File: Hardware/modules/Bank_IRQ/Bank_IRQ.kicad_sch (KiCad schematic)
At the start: 28 parts, among them J1 Ports, J2 Bus_PCI_6502, U1 74HC00, U2 74HC138, U3 6525

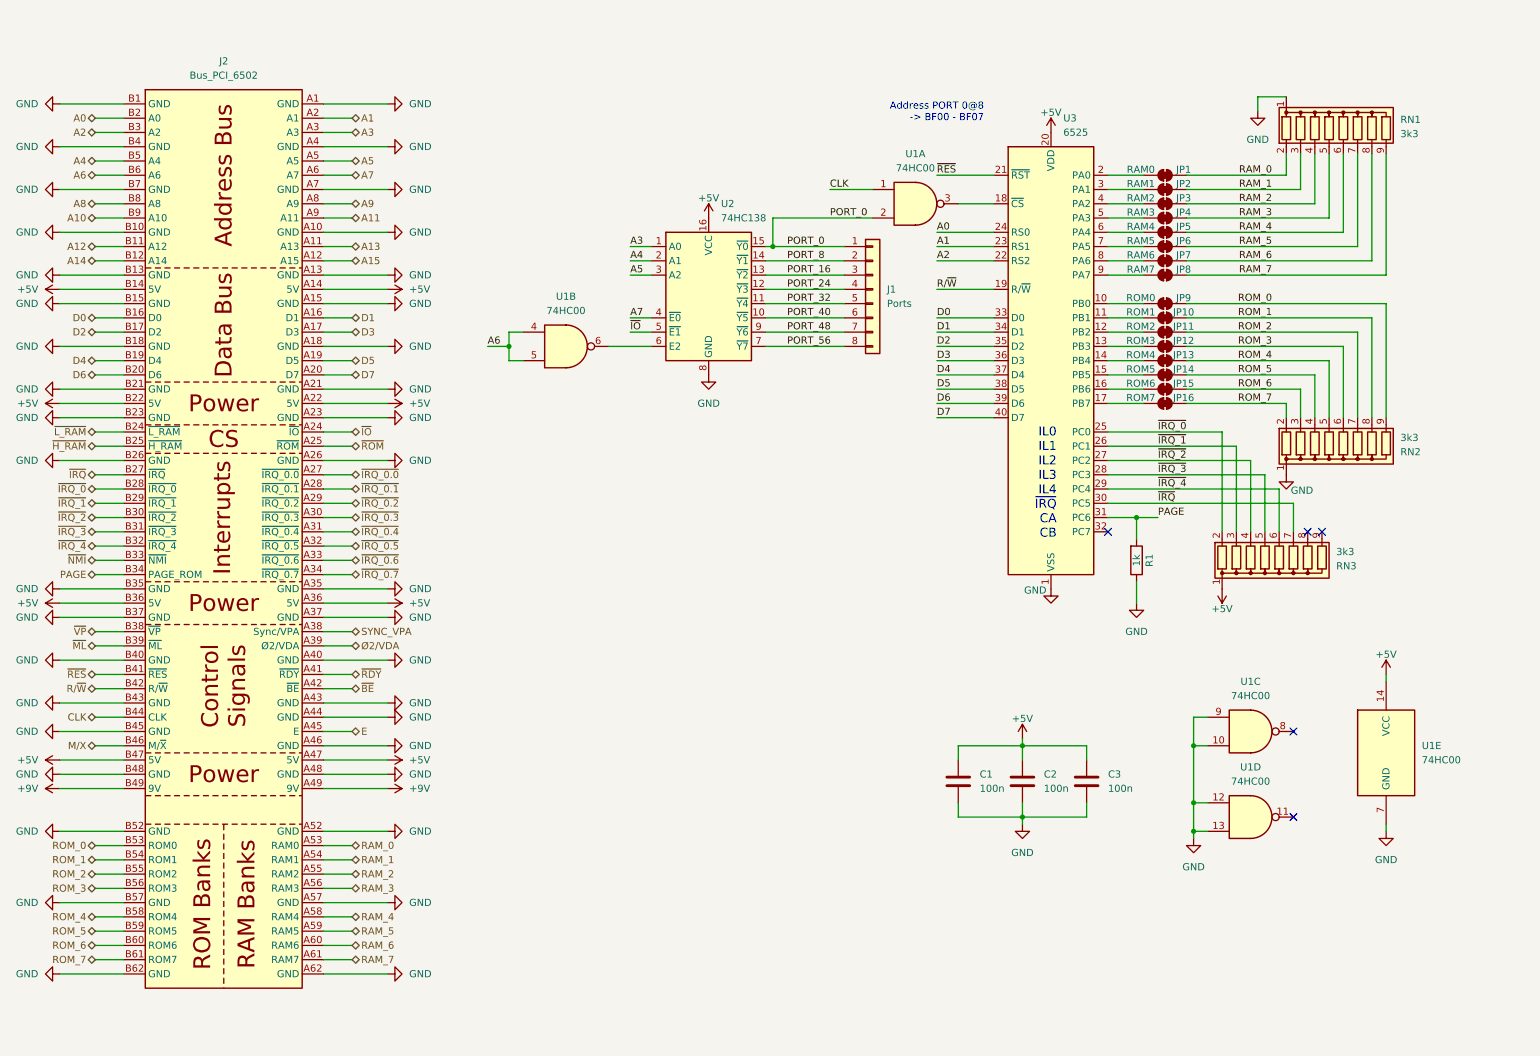
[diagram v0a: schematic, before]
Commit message: Hardware Update Add MyCPU VGA Module Beautify all Schematics minor Error corrections Readme Update
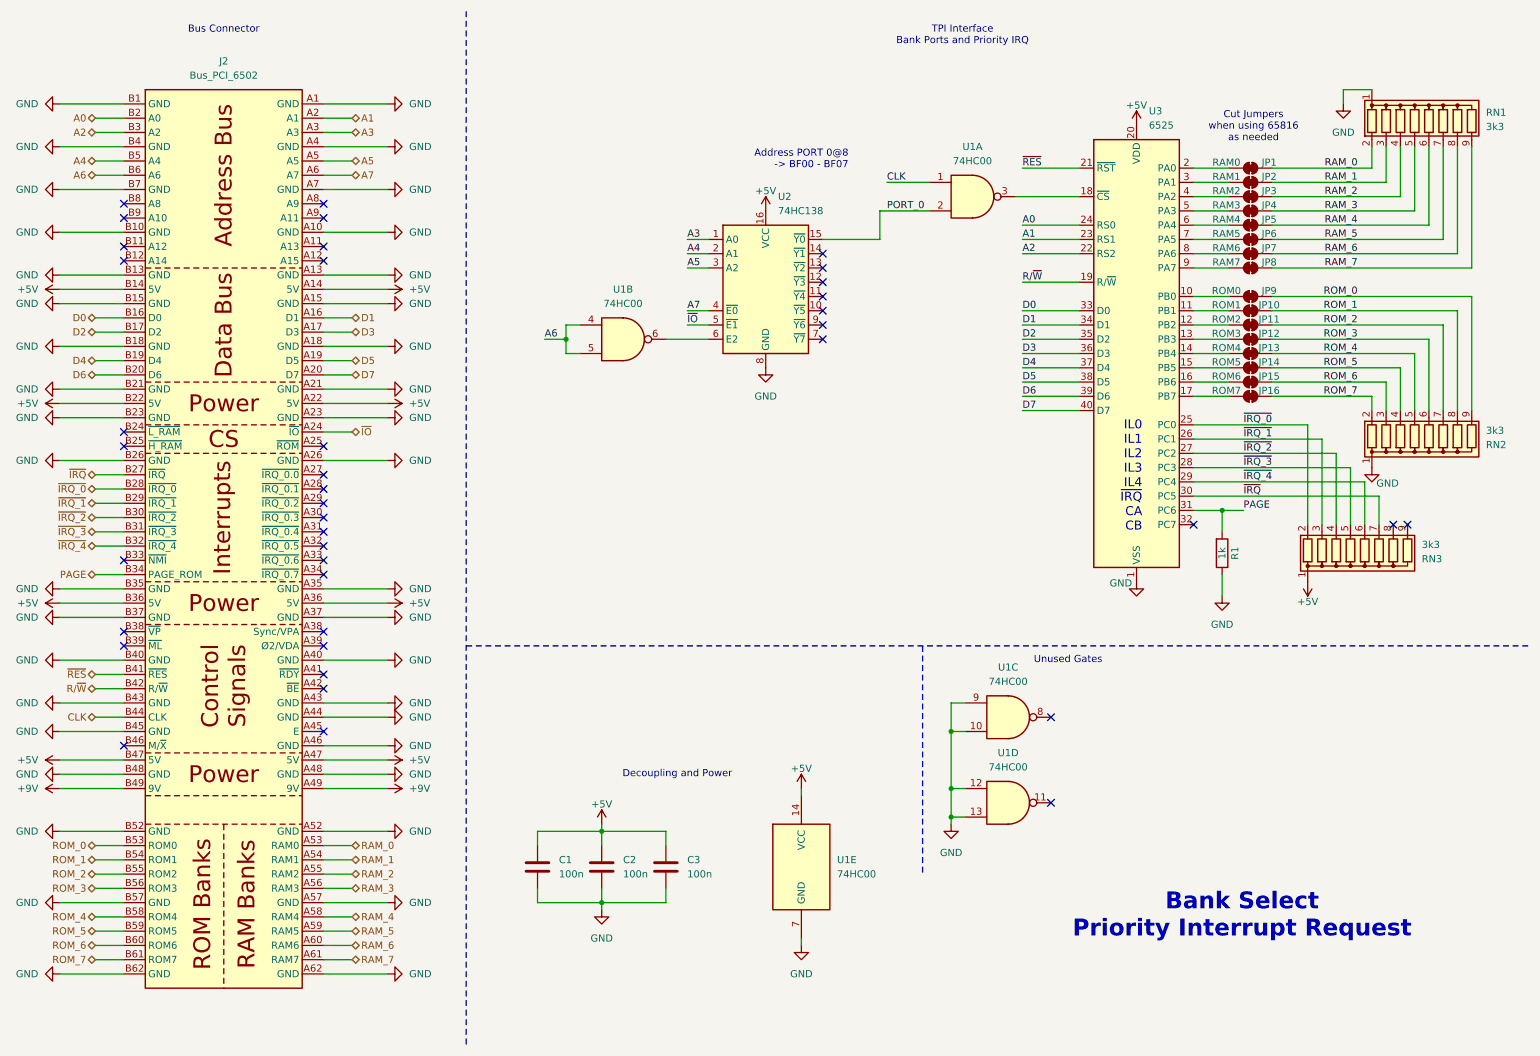
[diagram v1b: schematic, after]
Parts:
- removed J1: Ports, Connector_PinHeader_2.54mm:PinHeader_1x08_P2.54mm_Vertical, symbol Connector_Generic:Conn_01x08
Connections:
- net A10: no longer names the net of J2.B9 (A10)
- net A11: no longer names the net of J2.A9 (A11)
- net A12: no longer names the net of J2.B11 (A12)
- net A13: no longer names the net of J2.A11 (A13)
- net A14: no longer names the net of J2.B12 (A14)
- net A15: no longer names the net of J2.A12 (A15)
- net A8: no longer names the net of J2.B8 (A8)
- net A9: no longer names the net of J2.A8 (A9)
- net E: no longer names the net of J2.A45 (E)
- net M/X: no longer names the net of J2.B46 (M/~{X})
- net PORT_16: no longer names the net of U2.13 (~{Y2})
- net PORT_24: no longer names the net of U2.12 (~{Y3})
- net PORT_32: no longer names the net of U2.11 (~{Y4})
- net PORT_40: no longer names the net of U2.10 (~{Y5})
- net PORT_48: no longer names the net of U2.9 (~{Y6})
- net PORT_56: no longer names the net of U2.7 (~{Y7})
- net PORT_8: no longer names the net of U2.14 (~{Y1})
- net SYNC_VPA: no longer names the net of J2.A38 (Sync/VPA)
- net ~{BE}: no longer names the net of J2.A42 (~{BE})
- net ~{H_RAM}: no longer names the net of J2.B25 (~{H_RAM})
- net ~{IRQ_0.0}: no longer names the net of J2.A27 (~{IRQ_0.0})
- net ~{IRQ_0.1}: no longer names the net of J2.A28 (~{IRQ_0.1})
- net ~{IRQ_0.2}: no longer names the net of J2.A29 (~{IRQ_0.2})
- net ~{IRQ_0.3}: no longer names the net of J2.A30 (~{IRQ_0.3})
- net ~{IRQ_0.4}: no longer names the net of J2.A31 (~{IRQ_0.4})
- net ~{IRQ_0.5}: no longer names the net of J2.A32 (~{IRQ_0.5})
- net ~{IRQ_0.6}: no longer names the net of J2.A33 (~{IRQ_0.6})
- net ~{IRQ_0.7}: no longer names the net of J2.A34 (~{IRQ_0.7})
- net ~{L_RAM}: no longer names the net of J2.B24 (~{L_RAM})
- net ~{ML}: no longer names the net of J2.B39 (~{ML})
- net ~{NMI}: no longer names the net of J2.B33 (~{NMI})
- net ~{RDY}: no longer names the net of J2.A41 (~{RDY})
- net ~{ROM}: no longer names the net of J2.A25 (~{ROM})
- net ~{VP}: no longer names the net of J2.B38 (~{VP})
- net Ø2/VDA: no longer names the net of J2.A39 (Ø2/VDA)
- no-connect marks 5 -> 40
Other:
- note added: "Bank Select Priority Interrupt Request"
- note added: "Bus Connector"
- note added: "Cut Jumpers when using 65816 as needed"
- note added: "Decoupling and Power"
- note added: "TPI Interface Bank Ports and Priority IRQ"
- note added: "Unused Gates"
- company: (none) -> Synthron
- title: (none) -> S65xx Computer System
- moved on the sheet: C1, C2, C3, JP1, JP10, JP11, JP12, JP13, JP14, JP15, JP16, JP2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

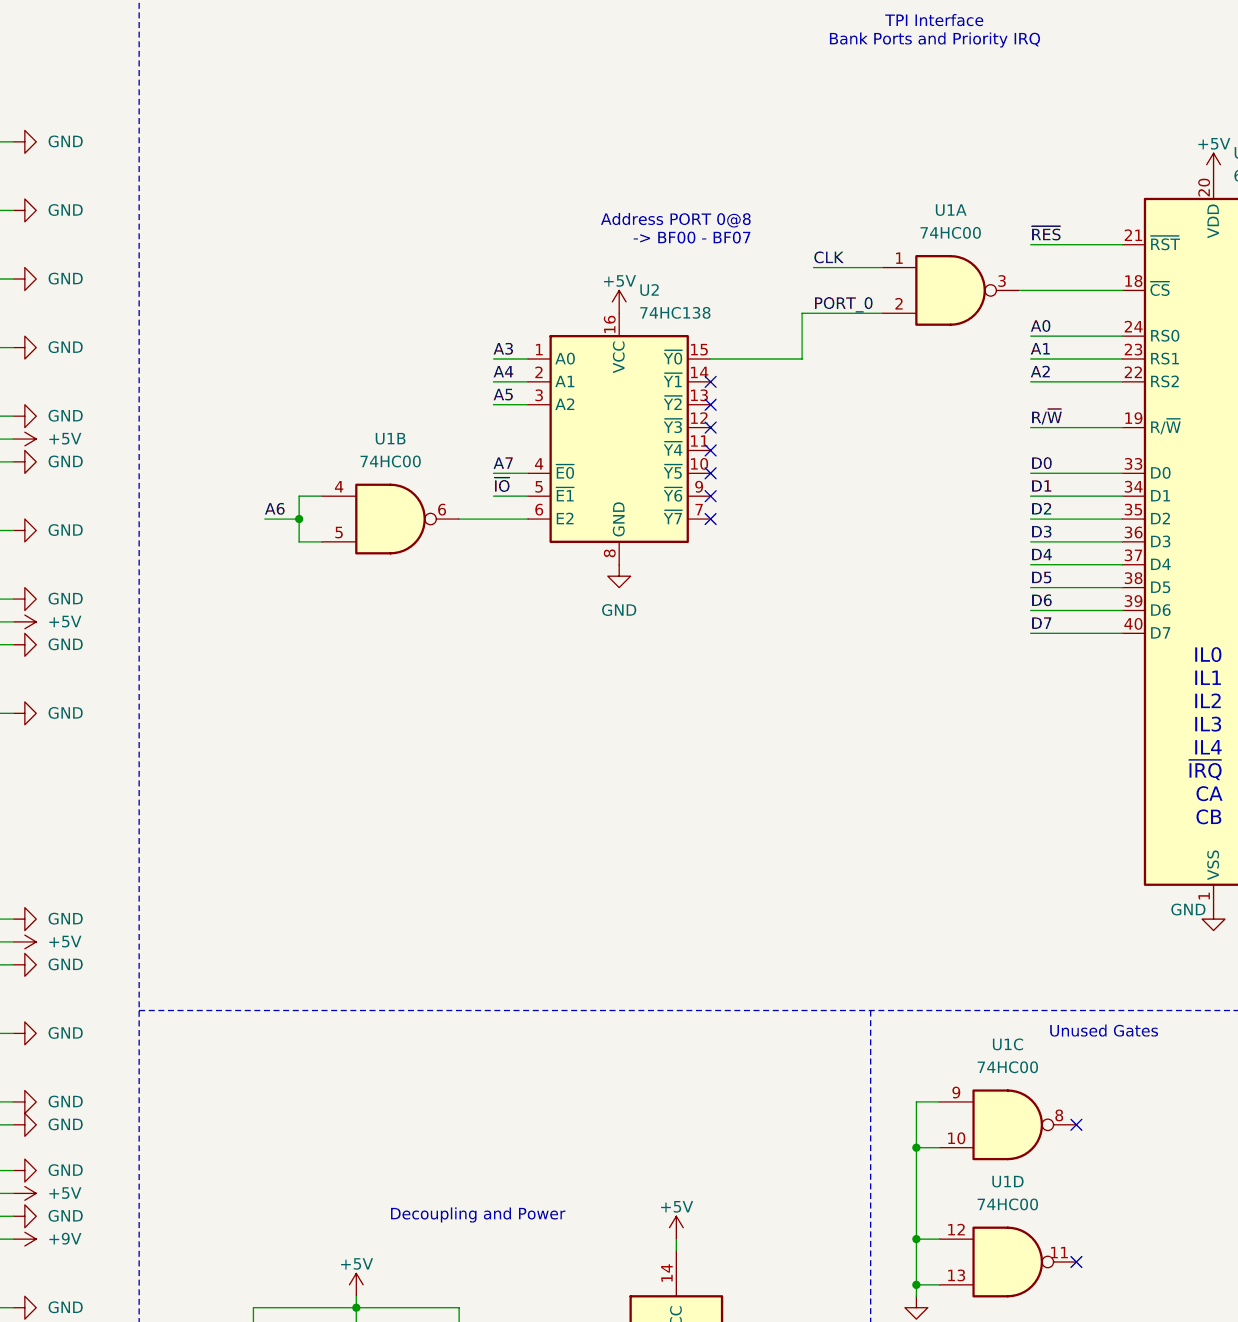
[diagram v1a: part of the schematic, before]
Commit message: Chip Select Strobe Generation Bugfix
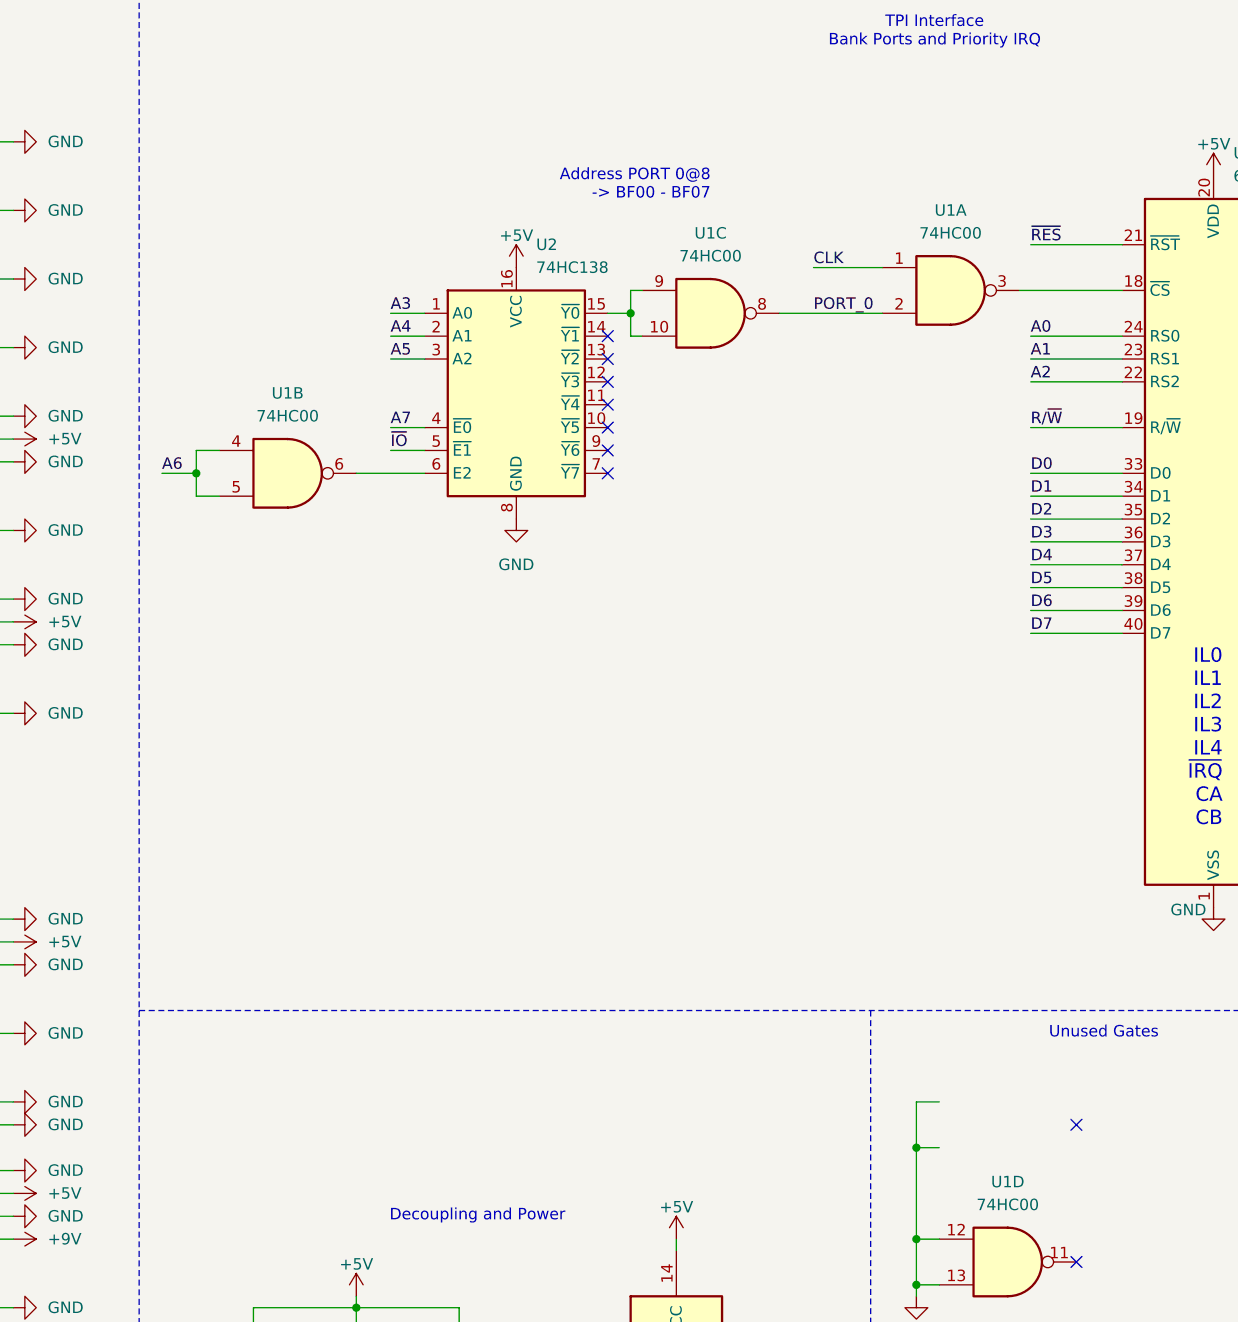
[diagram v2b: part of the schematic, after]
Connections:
- net GND: no longer U1.10, U1.9
- net PORT_0: now also U1.8; no longer U2.15 (~{Y0})
- new net: U1.10, U1.9, U2.15 (~{Y0})
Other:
- moved on the sheet: U1B, U1C, U2
